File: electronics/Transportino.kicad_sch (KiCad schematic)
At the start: 45 parts

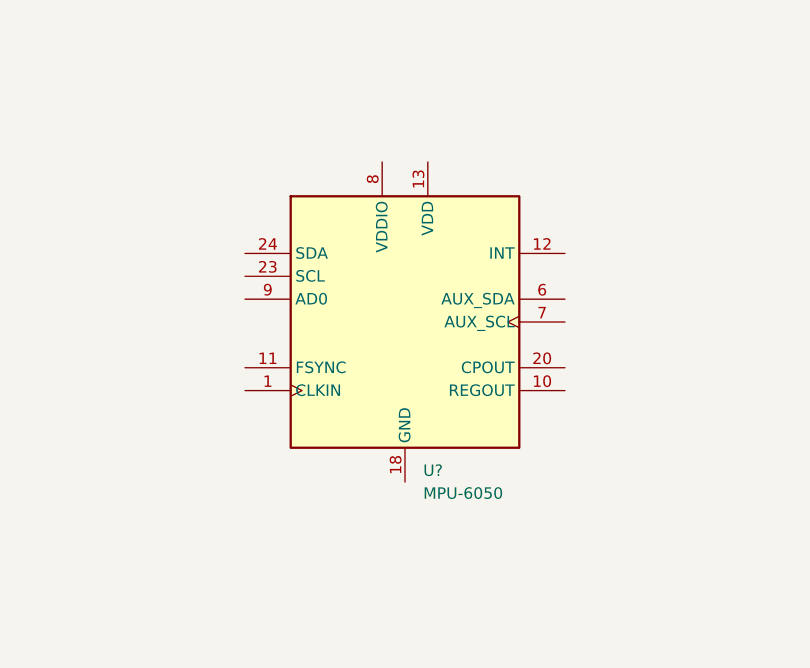
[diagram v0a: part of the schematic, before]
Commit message: Removed MPU6050 symbol
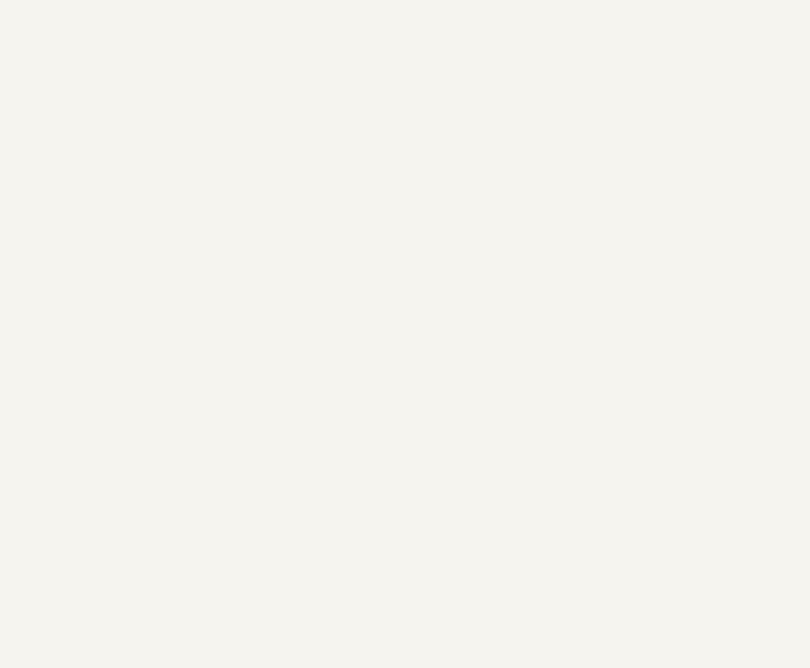
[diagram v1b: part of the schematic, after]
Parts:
- removed U?: MPU-6050, Sensor_Motion:InvenSense_QFN-24_4x4mm_P0.5mm, symbol Sensor_Motion:MPU-6050
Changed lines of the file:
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@@
     (pin "2")
-  )
-  (symbol (lib_id "Sensor_Motion:MPU-6050") (at 243.84 194.31 0) (unit 1)
-    (in_bom yes) (on_board yes) (fields_autoplaced)
-    (property "Reference" "U?" (id 0) (at 245.8594 210.82 0)
-      (effects (font (size 1.27 1.27)) (justify left))
-    )
-    (property "Value" "MPU-6050" (id 1) (at 245.8594 213.36 0)
-      (effects (font (size 1.27 1.27)) (justify left))
-    )
-    (property "Footprint" "Sensor_Motion:InvenSense_QFN-24_4x4mm_P0.5mm" (id 2) (at 243.84 214.63 0)
-      (effects (font (size 1.27 1.27)) hide)
-    )
-    (property "Datasheet" "https://store.invensense.com/datasheets/invensense/MPU-6050_DataSheet_V3%204.pdf" (id 3) (at 243.84 198.12 0)
-      (effects (font (size 1.27 1.27)) hide)
-    )
-    (pin "1")
-    (pin "10")
-    (pin "11")
-    (pin "12")
-    (pin "13")
-    (pin "14")
-    (pin "15")
-    (pin "16")
-    (pin "17")
-    (pin "18")
-    (pin "19")
-    (pin "2")
-    (pin "20")
-    (pin "21")
-    (pin "22")
-    (pin "23")
-    (pin "24")
-    (pin "3")
-    (pin "4")
-    (pin "5")
-    (pin "6")
-    (pin "7")
-    (pin "8")
-    (pin "9")
   )
   (symbol (lib_id "power:VBUS") (at 266.7 33.02 90) (unit 1)
@@
       (reference "U?") (unit 1) (value "NCP1117-3.3_SOT223") (footprint "Package_TO_SOT_SMD:SOT-223-3_TabPin2")
     )
-    (path "/8cf9d204-8c0f-4ba4-9cbf-1cc52872f2d2"
-      (reference "U?") (unit 1) (value "MPU-6050") (footprint "Sensor_Motion:InvenSense_QFN-24_4x4mm_P0.5mm")
-    )
     (path "/a53d9df3-45fe-482d-b79d-fa45ec3590ce"
